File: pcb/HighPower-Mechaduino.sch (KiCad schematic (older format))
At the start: 51 parts, among them J1 SUPPLY, J2 STEPPER, P1 SWD, P4 -, P5 -, P6 -, P7 -, Q1 SSM3J328R, Q2 BSS138, SW1 SW_PUSH, U1 AS5047D, U2 AP2112K-3.3TRG1, U3 AT24CS64-SSHM

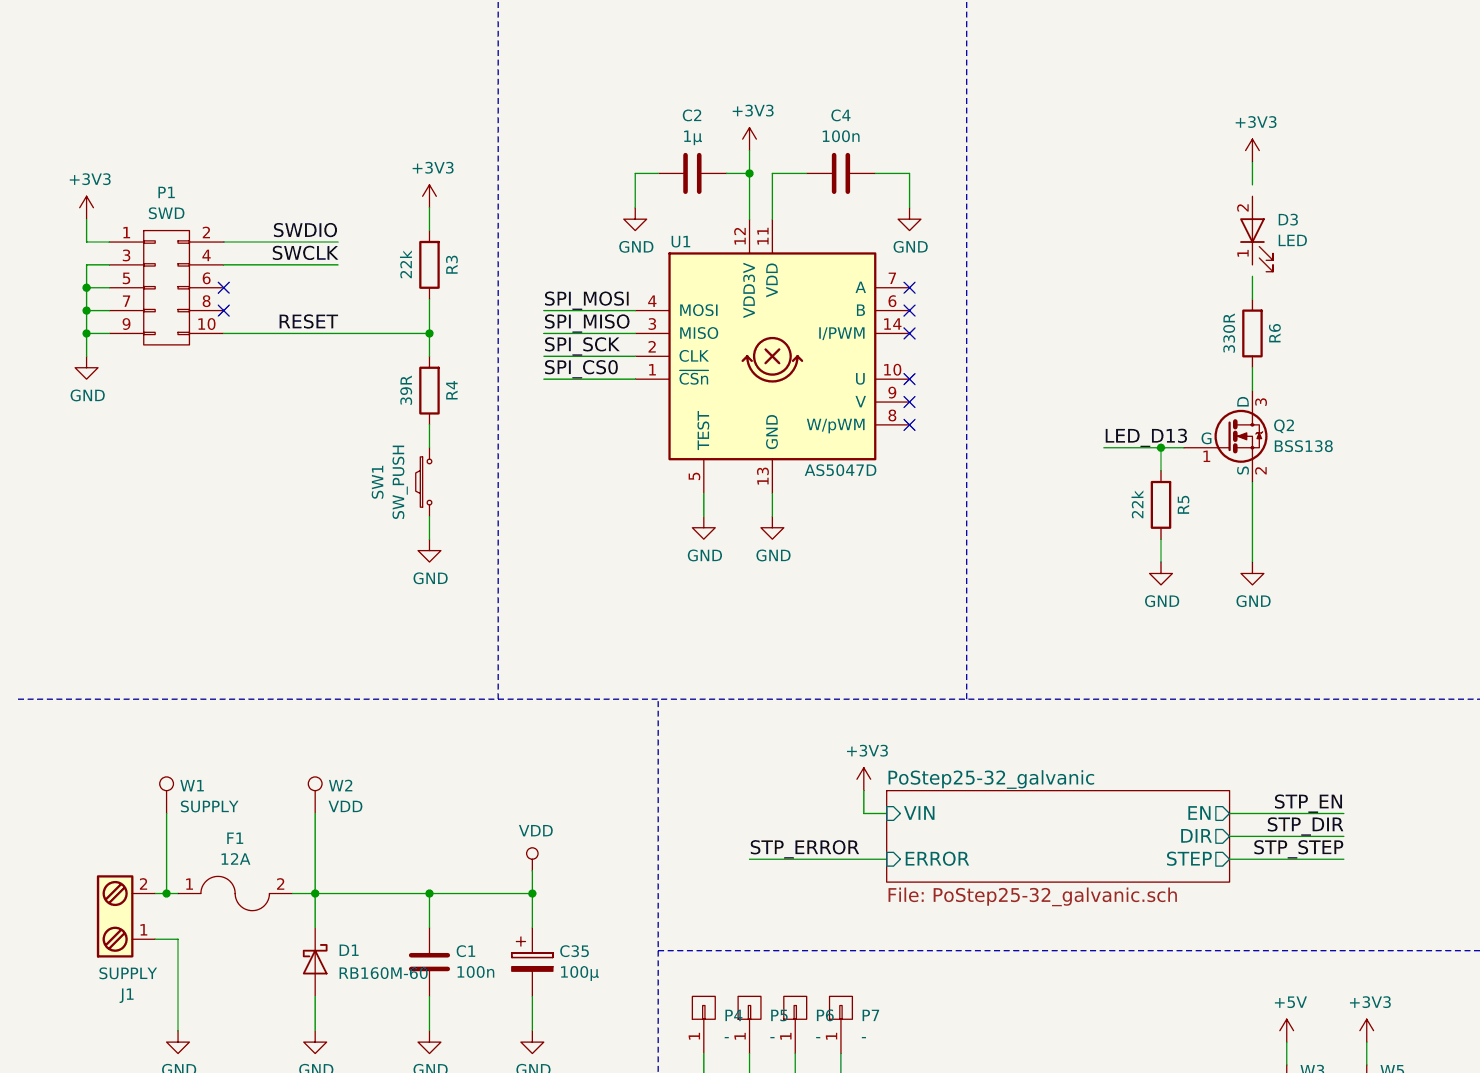
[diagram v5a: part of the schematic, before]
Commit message: Use new library symbols
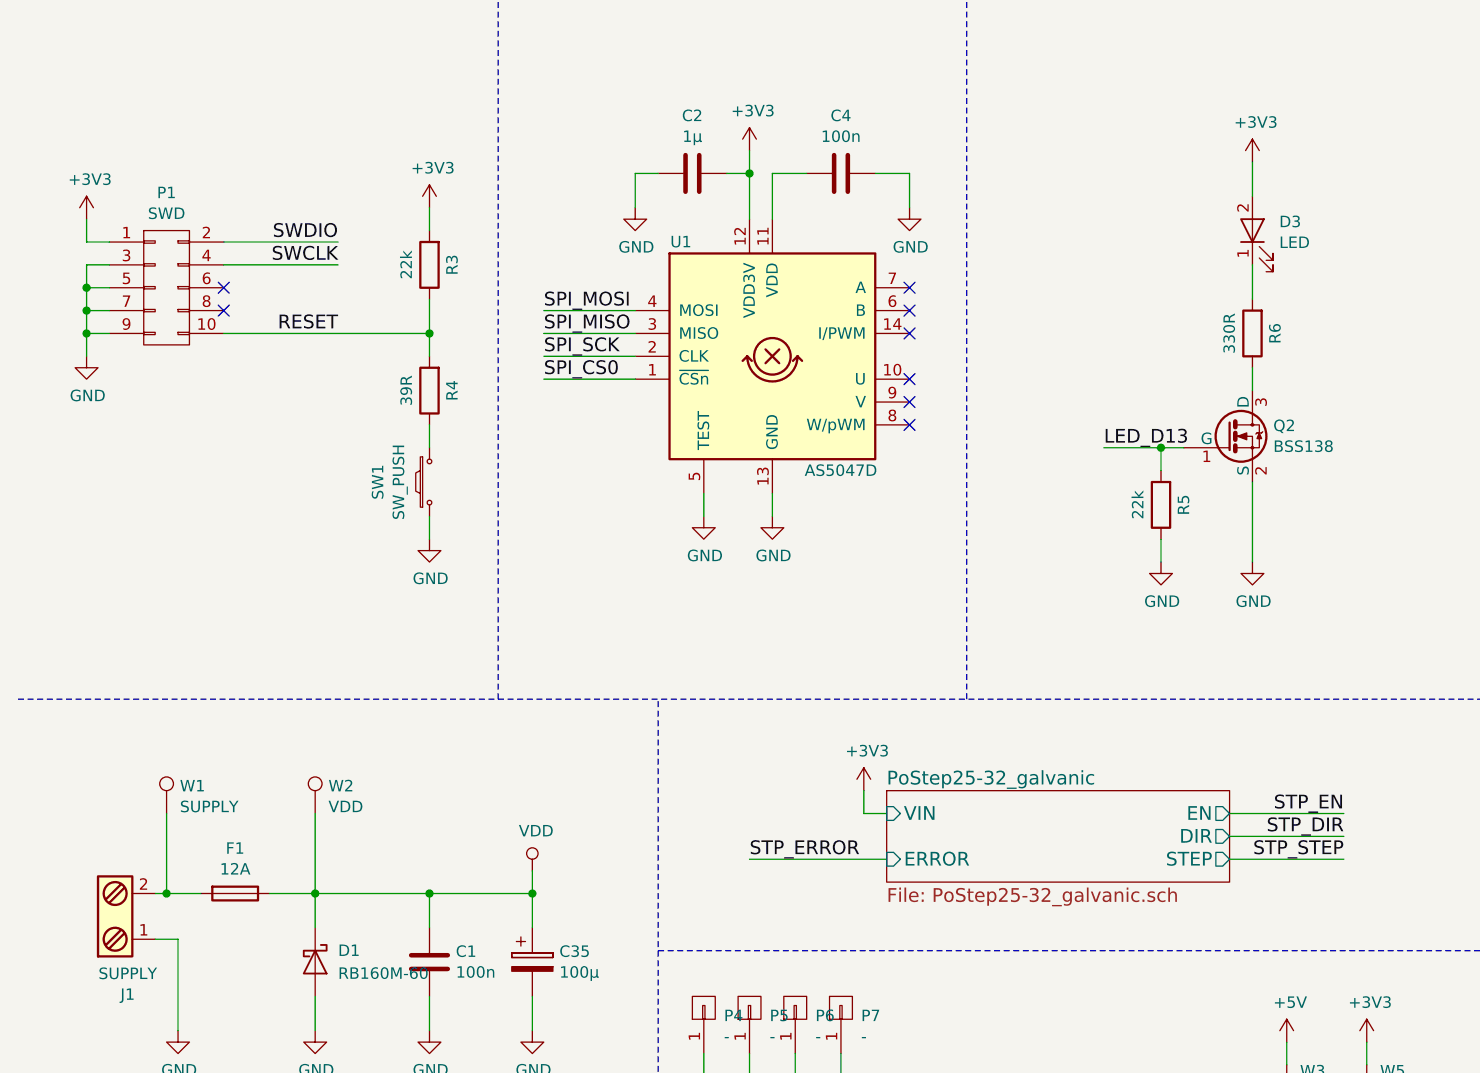
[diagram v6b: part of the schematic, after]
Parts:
- removed F1: 12A, Fuse_Holders_and_Fuses_local:Fuse_0679H, symbol FUSE
- added F1: 12A, Fuse_Holders_and_Fuses_local:Fuse_0679H, symbol Fuse
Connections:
- net +3V3: now also D3.2 (A)
- net VDD: now also F1.1
- net at J1.2, W1.1: now also F1.2
- net at R6.2: now also D3.1 (K)
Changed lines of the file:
@@
-$EndComp
-$Comp
-L FUSE F1
-U 1 1 580B492B
-P 1450 4450
-F 0 "F1" H 1450 4690 50  0000 C CNN
-F 1 "12A" H 1450 4599 50  0000 C CNN
-F 2 "Fuse_Holders_and_Fuses_local:Fuse_0679H" H 1450 4450 50  0001 C CNN
-F 3 "http://belfuse.com/pdfs/0679H.pdf" H 1450 4450 50  0001 C CNN
-F 4 "507-2059-6-ND" H 1450 4450 60  0001 C CNN "Digi-Key Part Number"
-F 5 "1" H 1450 4450 60  0001 C CNN "Digi-Key Minimum Quantity"
-	1    1450 4450
-	1    0    0    -1
 $EndComp
 $Comp
@@
 	1    5900 3000
 	1    0    0    -1
-$EndComp
-$Comp
-L LED D3
-U 1 1 580DA58F
-P 5900 1550
-F 0 "D3" V 5946 1442 50  0000 R CNN
-F 1 "LED" V 5855 1442 50  0000 R CNN
-F 2 "LEDs:LED_0805" H 5900 1550 50  0001 C CNN
-F 3 "" H 5900 1550 50  0000 C CNN
-	1    5900 1550
-	0    -1   -1   0
 $EndComp
 $Comp
@@
 	1200 4650 1200 5050
 Wire Wire Line
-	1100 4450 1200 4450
-Wire Wire Line
-	1700 4450 2750 4450
+	1100 4450 1300 4450
+Wire Wire Line
+	1600 4450 2750 4450
 Wire Wire Line
 	1800 4100 1800 4600
@@
 	5900 2250 5900 2150
 Wire Wire Line
-	5900 1850 5900 1750
-Wire Wire Line
-	5900 1250 5900 1350
+	5900 1700 5900 1850
+Wire Wire Line
+	5900 1250 5900 1400
 Connection ~ 5500 2500
 Wire Wire Line
@@
 Text Notes 7800 1450 0    60   ~ 0
 I_MAX = 14A
+$Comp
+L LED D3
+U 1 1 582E4EB6
+P 5900 1550
+F 0 "D3" V 5938 1433 50  0000 R CNN
+F 1 "LED" V 5847 1433 50  0000 R CNN
+F 2 "LEDs:LED_0805" V 5801 1433 50  0001 R CNN
+F 3 "" H 5900 1550 50  0000 C CNN
+	1    5900 1550
+	0    -1   -1   0
+$EndComp
+$Comp
+L Fuse F1
+U 1 1 582E7448
+P 1450 4450
+F 0 "F1" V 1253 4450 50  0000 C CNN
+F 1 "12A" V 1344 4450 50  0000 C CNN
+F 2 "Fuse_Holders_and_Fuses_local:Fuse_0679H" V 1345 4450 50  0001 C CNN
+F 3 "http://belfuse.com/pdfs/0679H.pdf" V 1345 4450 50  0001 C CNN
+F 4 "507-2059-6-ND" H 1450 4450 60  0001 C CNN "Digi-Key Part Number"
+F 5 "1" H 1450 4450 60  0001 C CNN "Digi-Key Minimum Quantity"
+	1    1450 4450
+	0    1    1    0
+$EndComp
 $EndSCHEMATC

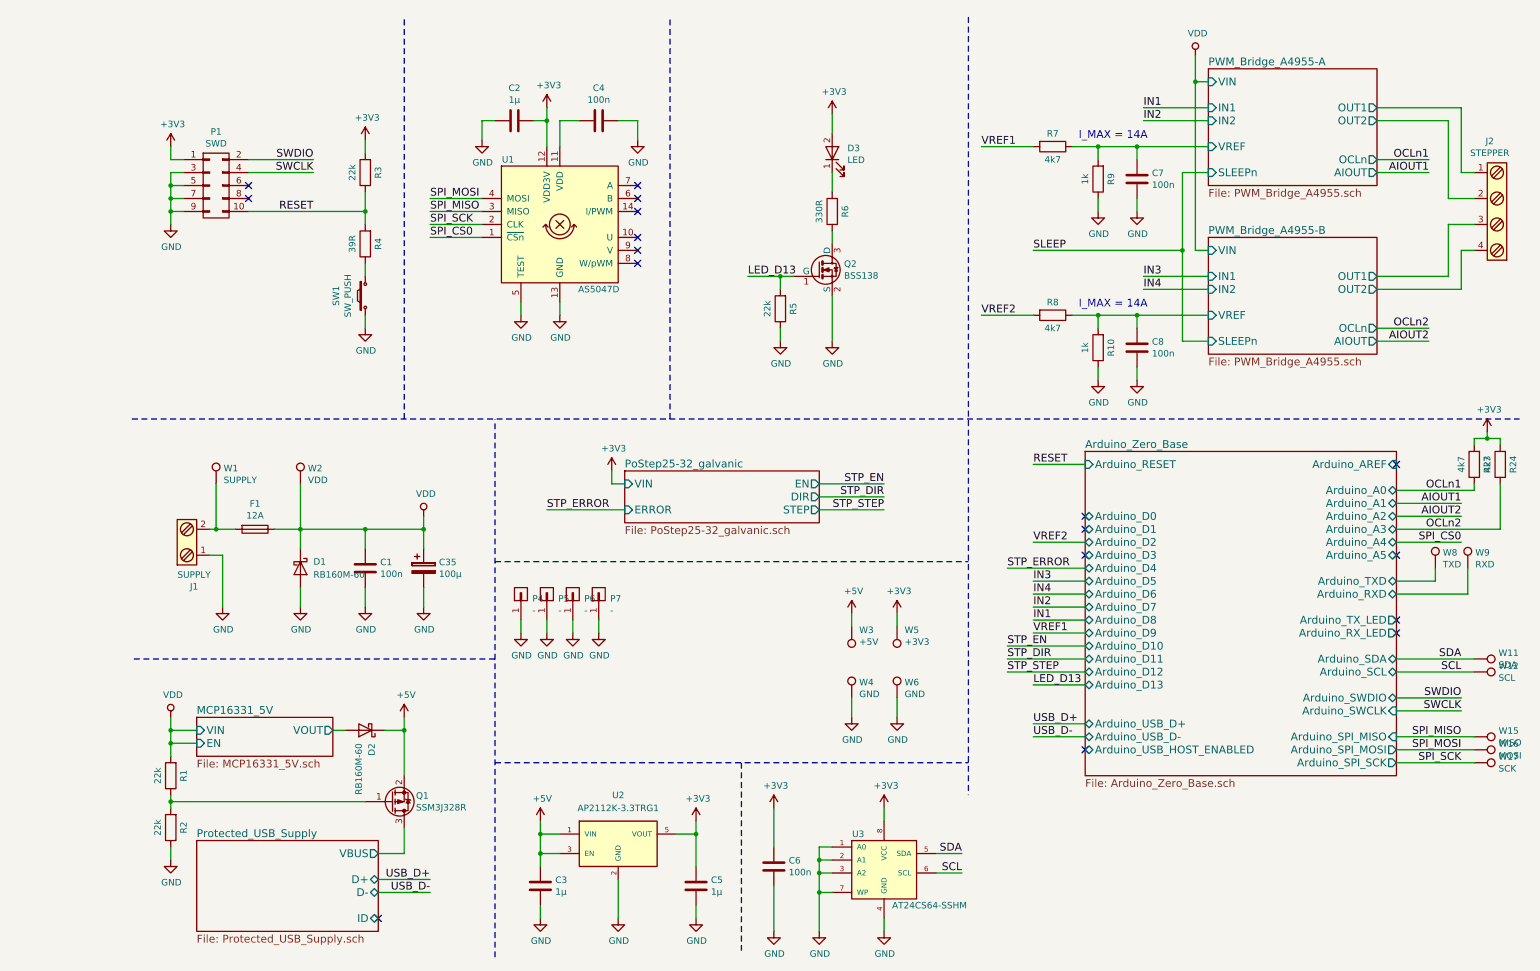
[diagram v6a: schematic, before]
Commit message: Improve layout and add voltage sensing circuit to layout
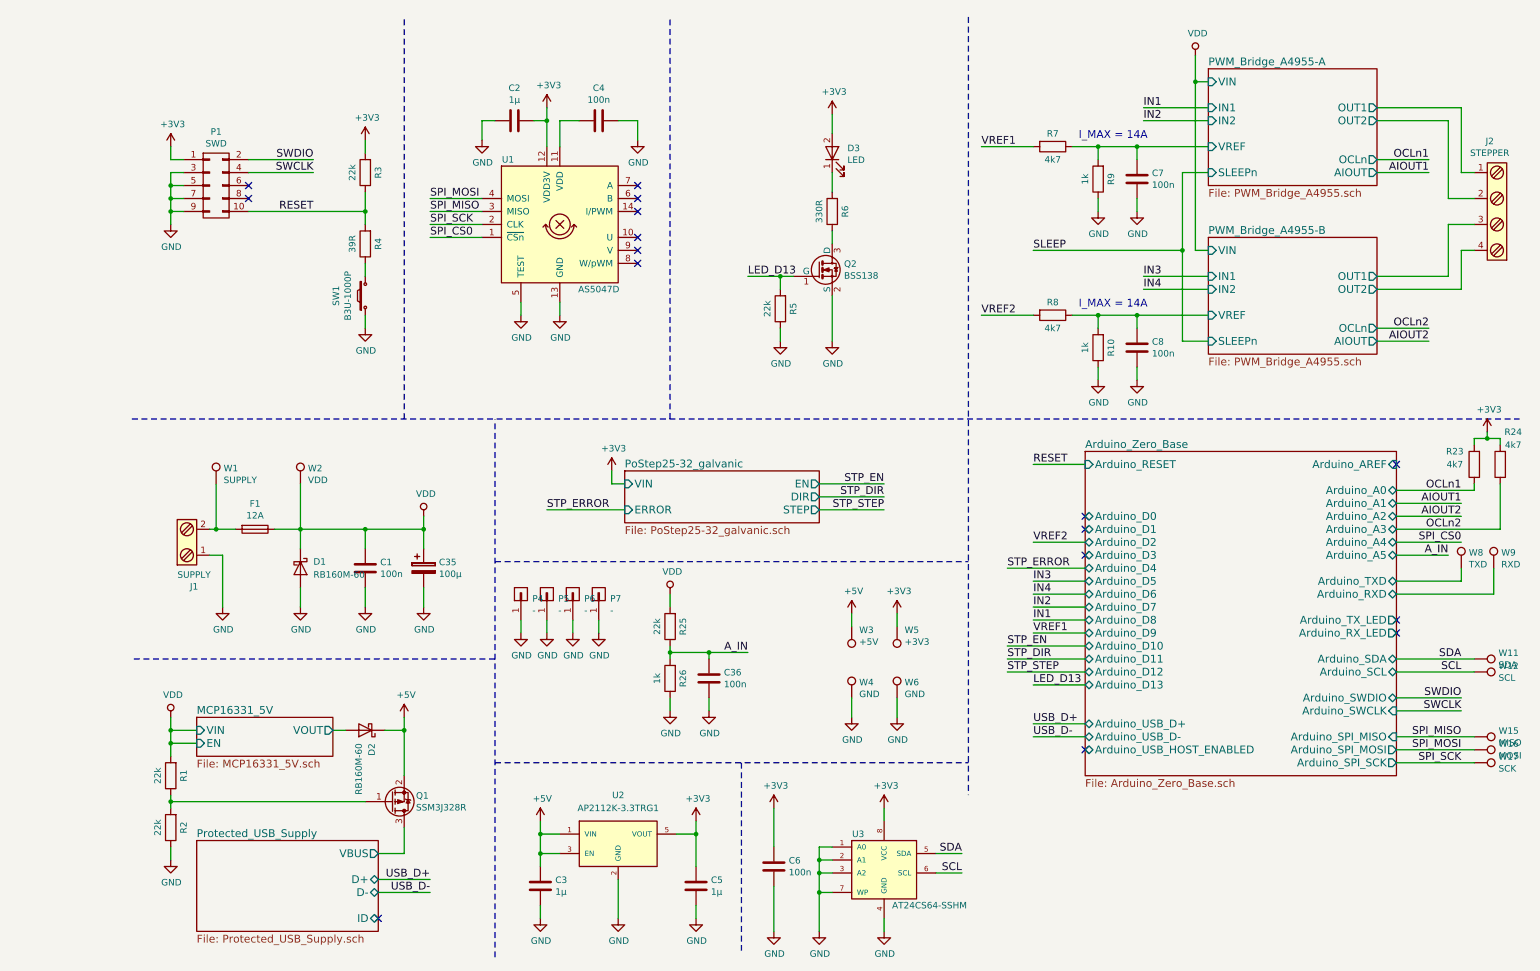
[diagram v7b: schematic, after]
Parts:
- added C36: 100n, Capacitors_SMD:C_0603, symbol C
- added R25: 22k, Resistors_SMD:R_0603, symbol R
- added R26: 1k, Resistors_SMD:R_0603, symbol R
- SW1: value SW_PUSH -> B3U-1000P
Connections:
- net GND: now also C36.1, R26.1
- net VDD: now also R25.2
- new net A_IN: C36.2, R25.1, R26.2
- no-connect marks 17 -> 16
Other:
- moved on the sheet: W8, W9
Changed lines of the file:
@@
 P 2300 2650
 F 0 "SW1" H 2300 2875 50  0000 C CNN
-F 1 "SW_PUSH" H 2300 2784 50  0000 C CNN
+F 1 "B3U-1000P" H 2300 2784 50  0000 C CNN
 F 2 "Buttons_Switches_SMD:SW_SPST_B3U-1000P" H 2300 2850 50  0001 C CNN
 F 3 "http://www.omron.com/ecb/products/pdf/en-b3u.pdf" H 2300 2850 50  0001 C CNN
@@
 NoConn ~ 10250 5250
 NoConn ~ 10250 5150
-NoConn ~ 10250 4650
 NoConn ~ 7850 4350
 NoConn ~ 7850 4450
@@
 L TEST_1P W8
 U 1 1 5816F3EA
-P 10550 4750
-F 0 "W8" H 10608 4870 50  0000 L CNN
-F 1 "TXD" H 10608 4779 50  0000 L CNN
-F 2 "Measurement_Points:Measurement_Point_Round-SMD-Pad_Small" H 10750 4750 50  0001 C CNN
-F 3 "" H 10750 4750 50  0000 C CNN
-	1    10550 4750
+P 10750 4750
+F 0 "W8" H 10808 4870 50  0000 L CNN
+F 1 "TXD" H 10808 4779 50  0000 L CNN
+F 2 "Measurement_Points:Measurement_Point_Round-SMD-Pad_Small" H 10950 4750 50  0001 C CNN
+F 3 "" H 10950 4750 50  0000 C CNN
+	1    10750 4750
 	1    0    0    -1
 $EndComp
@@
 L TEST_1P W9
 U 1 1 581716F2
-P 10800 4750
-F 0 "W9" H 10858 4870 50  0000 L CNN
-F 1 "RXD" H 10858 4779 50  0000 L CNN
-F 2 "Measurement_Points:Measurement_Point_Round-SMD-Pad_Small" H 11000 4750 50  0001 C CNN
-F 3 "" H 11000 4750 50  0000 C CNN
-	1    10800 4750
+P 11000 4750
+F 0 "W9" H 11058 4870 50  0000 L CNN
+F 1 "RXD" H 11058 4779 50  0000 L CNN
+F 2 "Measurement_Points:Measurement_Point_Round-SMD-Pad_Small" H 11200 4750 50  0001 C CNN
+F 3 "" H 11200 4750 50  0000 C CNN
+	1    11000 4750
 	1    0    0    -1
 $EndComp
@@
 Connection ~ 1150 4450
 Wire Wire Line
-	10250 4850 10550 4850
-Wire Wire Line
-	10550 4850 10550 4750
-Wire Wire Line
-	10250 4950 10800 4950
-Wire Wire Line
-	10800 4950 10800 4750
+	10250 4850 10750 4850
+Wire Wire Line
+	10750 4850 10750 4750
+Wire Wire Line
+	10250 4950 11000 4950
+Wire Wire Line
+	11000 4950 11000 4750
 Wire Wire Line
 	6400 5100 6400 5200
@@
 U 1 1 581F0CE8
 P 10850 3950
-F 0 "R23" V 10750 3950 50  0000 C CNN
-F 1 "4k7" V 10950 3950 50  0000 C CNN
+F 0 "R23" H 11000 3850 50  0000 C CNN
+F 1 "4k7" H 11000 3950 50  0000 C CNN
 F 2 "Resistors_SMD:R_0603" V 10780 3950 50  0001 C CNN
 F 3 "" H 10850 3950 50  0000 C CNN
@@
 U 1 1 581F164E
 P 11050 3950
-F 0 "R24" V 10950 3950 50  0000 C CNN
-F 1 "4k7" V 11150 3950 50  0000 C CNN
+F 0 "R24" H 10950 3700 50  0000 C CNN
+F 1 "4k7" H 10950 3800 50  0000 C CNN
 F 2 "Resistors_SMD:R_0603" V 10980 3950 50  0001 C CNN
 F 3 "" H 11050 3950 50  0000 C CNN
@@
 $EndComp
 Wire Wire Line
-	11050 3800 11050 3750
-Wire Wire Line
-	11050 3750 10850 3750
+	11050 3750 11050 3800
+Wire Wire Line
+	10850 3750 11050 3750
 Wire Wire Line
 	10850 3750 10850 3800
@@
 	0    1    1    0
 $EndComp
+$Comp
+L R R25
+U 1 1 5830B140
+P 4650 5200
+F 0 "R25" V 4550 5200 50  0000 C CNN
+F 1 "22k" V 4750 5200 50  0000 C CNN
+F 2 "Resistors_SMD:R_0603" V 4580 5200 50  0001 C CNN
+F 3 "" H 4650 5200 50  0000 C CNN
+F 4 "311-22.0KHRCT-ND" H 4650 5200 60  0001 C CNN "Digi-Key Part Number"
+F 5 "1" H 4650 5200 60  0001 C CNN "Digi-Key Minimum Quantity"
+	1    4650 5200
+	-1   0    0    1
+$EndComp
+$Comp
+L VDD #PWR046
+U 1 1 5830C24C
+P 4650 4950
+F 0 "#PWR046" H 4650 4800 50  0001 C CNN
+F 1 "VDD" H 4667 5123 50  0000 C CNN
+F 2 "" H 4650 4950 50  0000 C CNN
+F 3 "" H 4650 4950 50  0000 C CNN
+	1    4650 4950
+	1    0    0    -1
+$EndComp
+$Comp
+L GND #PWR047
+U 1 1 5830CF9B
+P 4650 5850
+F 0 "#PWR047" H 4650 5600 50  0001 C CNN
+F 1 "GND" H 4655 5677 50  0000 C CNN
+F 2 "" H 4650 5850 50  0000 C CNN
+F 3 "" H 4650 5850 50  0000 C CNN
+	1    4650 5850
+	1    0    0    -1
+$EndComp
+Wire Wire Line
+	4650 4950 4650 5050
+Wire Wire Line
+	4650 5350 4650 5450
+Wire Wire Line
+	4650 5750 4650 5850
+$Comp
+L R R26
+U 1 1 5830E429
+P 4650 5600
+F 0 "R26" V 4550 5600 50  0000 C CNN
+F 1 "1k" V 4750 5600 50  0000 C CNN
+F 2 "Resistors_SMD:R_0603" V 4580 5600 50  0001 C CNN
+F 3 "" H 4650 5600 50  0000 C CNN
+F 4 "311-1.00KHRCT-ND" H 4650 5600 60  0001 C CNN "Digi-Key Part Number"
+F 5 "1" H 4650 5600 60  0001 C CNN "Digi-Key Minimum Quantity"
+	1    4650 5600
+	-1   0    0    1
+$EndComp
+Wire Wire Line
+	4650 5400 5250 5400
+Connection ~ 4650 5400
+Text Label 5250 5400 2    60   ~ 0
+A_IN
+Wire Wire Line
+	10250 4650 10650 4650
+Text Label 10650 4650 2    60   ~ 0
+A_IN
+$Comp
+L C C36
+U 1 1 583121FE
+P 4950 5600
+F 0 "C36" H 4835 5554 50  0000 R CNN
+F 1 "100n" H 4835 5645 50  0000 R CNN
+F 2 "Capacitors_SMD:C_0603" H 4988 5450 50  0001 C CNN
+F 3 "" H 4950 5600 50  0000 C CNN
+F 4 "311-1343-1-ND" H 4950 5600 60  0001 C CNN "Digi-Key Part Number"
+F 5 "1" H 4950 5600 60  0001 C CNN "Digi-Key Minimum Quantity"
+	1    4950 5600
+	-1   0    0    1
+$EndComp
+$Comp
+L GND #PWR048
+U 1 1 58312EF9
+P 4950 5850
+F 0 "#PWR048" H 4950 5600 50  0001 C CNN
+F 1 "GND" H 4955 5677 50  0000 C CNN
+F 2 "" H 4950 5850 50  0000 C CNN
+F 3 "" H 4950 5850 50  0000 C CNN
+	1    4950 5850
+	1    0    0    -1
+$EndComp
+Wire Wire Line
+	4950 5450 4950 5400
+Connection ~ 4950 5400
+Wire Wire Line
+	4950 5750 4950 5850
 $EndSCHEMATC

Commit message: Add some improvements, fix issue with schematic error
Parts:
- removed D2: RB160M-60, Diodes_SMD:SOD-123, symbol D_Schottky
- added C37: 100n, Capacitors_SMD:C_0603, symbol C
- added U9: LM75BD, Housings_SOIC:SOIC-8_3.9x4.9mm_Pitch1.27mm, symbol LM75BD
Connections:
- net +3V3: now also C37.2, U9.8 (VCC)
- net GND: now also C37.1, U9.4 (GND), U9.5 (A2), U9.6 (A1), U9.7 (A0); no longer U3.4 (GND)
- net SCL: now also U9.2 (SCL)
- net SDA: now also U9.1 (SDA)
- no-connect marks 16 -> 17
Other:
- moved on the sheet: C1, C2, C3, C35, C36, C4, C5, D1, J1, P1, P4, P5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
